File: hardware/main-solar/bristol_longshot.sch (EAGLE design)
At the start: 83 parts, among them U1 SAM_D20E, U10 TPS62243, U11 TPS3808, U12 74LVC1G04GW, U13 SPV1040, U14 LT4054ES5-4.2, U2 SI4060, U3 UBLOX_MAX, U4 TPS62243, U5 TG-5006CJ, U6 TG-5006CJ, U7 TPS3123, U8 SN74LVC1G32DCKR, U9 SE880, Y1 ABS05

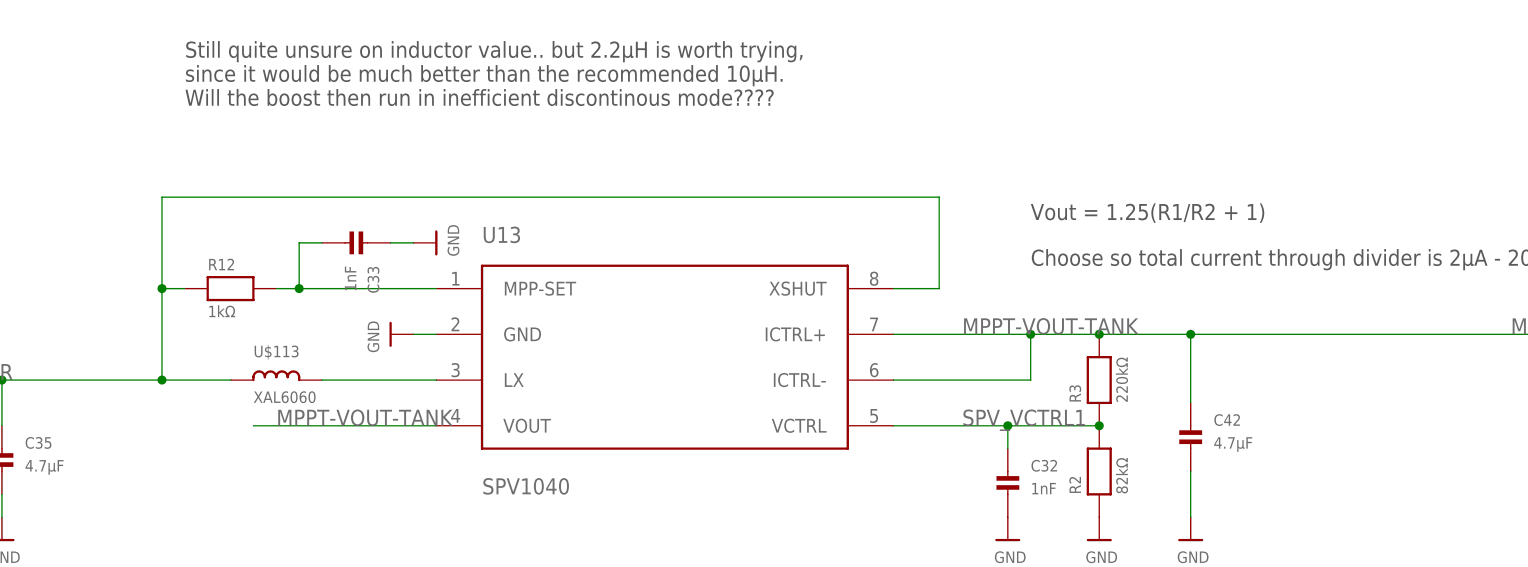
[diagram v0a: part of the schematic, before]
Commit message: Added LPS3015 mppt inductor footprint alongside XAL6060 footprint
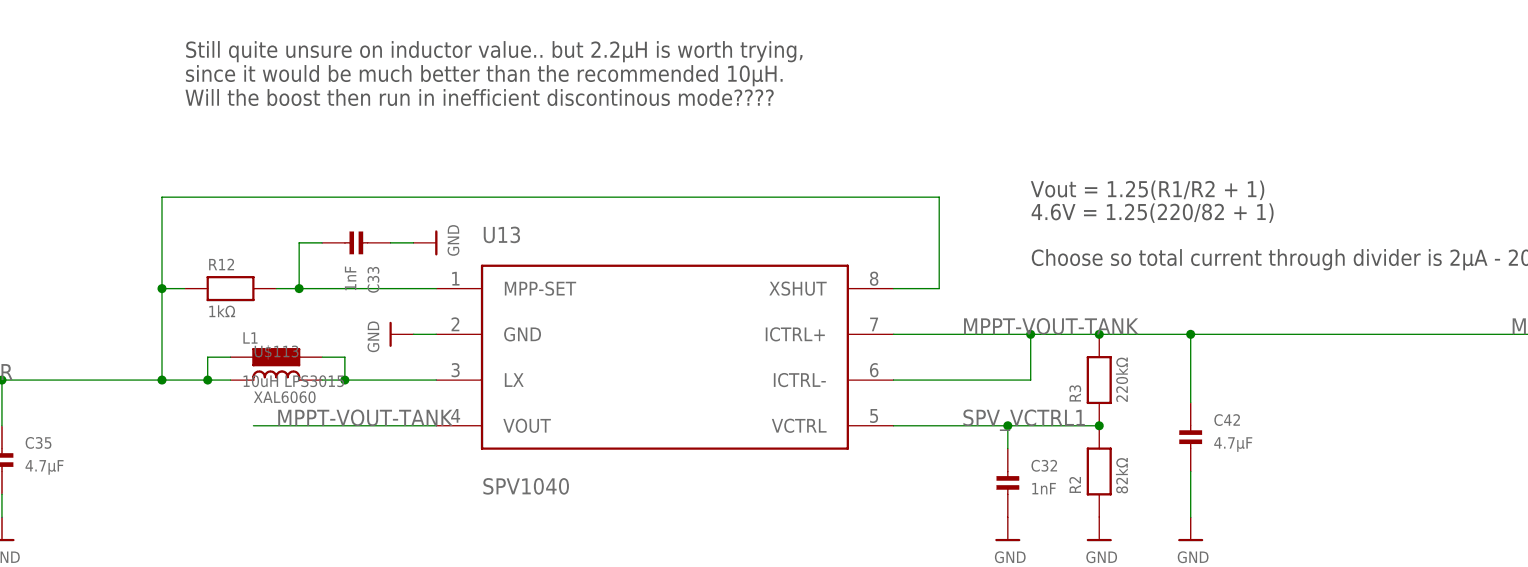
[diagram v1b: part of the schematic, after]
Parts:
- added L1: 10uH LPS3015, PecanFemto4:IND-LPS3015
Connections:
- net LX1: now also L1.2
- net VSOLAR: now also L1.1
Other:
- note added: "4.6V = 1.25(220/82 + 1)"
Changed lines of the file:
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@@
 <layer number="54" name="bGND_GNDA" color="1" fill="9" visible="no" active="no"/>
 <layer number="56" name="wert" color="7" fill="1" visible="no" active="no"/>
+<layer number="57" name="tCAD" color="7" fill="1" visible="no" active="no"/>
 <layer number="90" name="Modules" color="5" fill="1" visible="yes" active="yes"/>
 <layer number="91" name="Nets" color="2" fill="1" visible="yes" active="yes"/>
@@
 <layer number="97" name="Info" color="7" fill="1" visible="yes" active="yes"/>
 <layer number="98" name="Guide" color="6" fill="1" visible="yes" active="yes"/>
+<layer number="99" name="SpiceOrder" color="7" fill="1" visible="yes" active="yes"/>
 <layer number="100" name="Muster" color="7" fill="1" visible="no" active="no"/>
 <layer number="101" name="Patch_Top" color="12" fill="4" visible="yes" active="yes"/>
@@
 <layer number="111" name="LPC17xx" color="7" fill="1" visible="yes" active="yes"/>
 <layer number="112" name="tSilk" color="7" fill="1" visible="yes" active="yes"/>
+<layer number="113" name="IDFDebug" color="4" fill="1" visible="yes" active="yes"/>
 <layer number="116" name="Patch_BOT" color="9" fill="4" visible="yes" active="yes"/>
 <layer number="121" name="_tsilk" color="7" fill="1" visible="yes" active="yes"/>
@@
 <layer number="132" name="bAdjust" color="7" fill="1" visible="no" active="yes"/>
 <layer number="144" name="Drill_legend" color="7" fill="1" visible="yes" active="yes"/>
+<layer number="150" name="Notes" color="7" fill="1" visible="yes" active="yes"/>
 <layer number="151" name="HeatSink" color="7" fill="1" visible="yes" active="yes"/>
 <layer number="152" name="_bDocu" color="7" fill="1" visible="yes" active="yes"/>
+<layer number="153" name="FabDoc1" color="7" fill="1" visible="yes" active="yes"/>
+<layer number="154" name="FabDoc2" color="7" fill="1" visible="yes" active="yes"/>
+<layer number="155" name="FabDoc3" color="7" fill="1" visible="yes" active="yes"/>
 <layer number="199" name="Contour" color="7" fill="1" visible="yes" active="yes"/>
 <layer number="200" name="200bmp" color="1" fill="10" visible="no" active="no"/>
@@
 <part name="C42" library="microbuilder_v3" deviceset="CAP_CERAMIC" device="_0402" value="4.7µF"/>
 <part name="R21" library="microbuilder_v3" deviceset="RESISTOR" device="_0402" value="DNP"/>
+<part name="L1" library="PecanFemto4" deviceset="IND-LPS3015" device="" value="10uH LPS3015"/>
 </parts>
 <sheets>
@@
 <text x="347.98" y="-114.3" size="1.778" layer="97">Rchg = 2.2kΩ gives Ichg = 70mA</text>
 <text x="347.98" y="-119.38" size="1.778" layer="97">Ichg can be measured by Vprog</text>
-<text x="165.1" y="-45.72" size="1.778" layer="97">Vout = 1.25(R1/R2 + 1)</text>
+<text x="165.1" y="-43.18" size="1.778" layer="97">Vout = 1.25(R1/R2 + 1)</text>
 <text x="165.1" y="-50.8" size="1.778" layer="97">Choose so total current through divider is 2µA - 20µA</text>
 <text x="7.62" y="-50.8" size="1.778" layer="97">Not actually an SMA connector</text>
 <text x="96.52" y="81.788" size="1.27" layer="97" font="vector" ratio="11">(AIN[0])</text>
 <text x="96.52" y="76.708" size="1.27" layer="97" font="vector" ratio="11">(AIN[4])</text>
+<text x="165.1" y="-45.72" size="1.778" layer="97">4.6V = 1.25(220/82 + 1)</text>
 </plain>
 <instances>
@@
 <instance part="C42" gate="G$1" x="182.88" y="-71.12"/>
 <instance part="R21" gate="G$1" x="378.46" y="-48.26"/>
+<instance part="L1" gate="G$1" x="81.28" y="-60.96"/>
 </instances>
 <busses>
@@
 <net name="VSOLAR" class="0">
 <segment>
-<wire x1="76.2" y1="-63.5" x2="68.58" y2="-63.5" width="0.1524" layer="91"/>
+<wire x1="76.2" y1="-63.5" x2="73.66" y2="-63.5" width="0.1524" layer="91"/>
 <label x="43.18" y="-63.5" size="1.778" layer="95"/>
 <pinref part="R12" gate="G$1" pin="1"/>
+<wire x1="73.66" y1="-63.5" x2="68.58" y2="-63.5" width="0.1524" layer="91"/>
 <wire x1="68.58" y1="-63.5" x2="50.8" y2="-63.5" width="0.1524" layer="91"/>
 <wire x1="50.8" y1="-63.5" x2="40.64" y2="-63.5" width="0.1524" layer="91"/>
@@
 <junction x="40.64" y="-63.5"/>
 <wire x1="25.4" y1="-63.5" x2="40.64" y2="-63.5" width="0.1524" layer="91"/>
+<pinref part="L1" gate="G$1" pin="1"/>
+<wire x1="76.2" y1="-60.96" x2="73.66" y2="-60.96" width="0.1524" layer="91"/>
+<wire x1="73.66" y1="-60.96" x2="73.66" y2="-63.5" width="0.1524" layer="91"/>
+<junction x="73.66" y="-63.5"/>
 </segment>
 <segment>
@@
 <segment>
 <pinref part="U13" gate="G$1" pin="LX"/>
-<wire x1="86.36" y1="-63.5" x2="99.06" y2="-63.5" width="0.1524" layer="91"/>
+<wire x1="86.36" y1="-63.5" x2="88.9" y2="-63.5" width="0.1524" layer="91"/>
 <pinref part="U$113" gate="G$1" pin="2"/>
-</segment>
-</net>
+<pinref part="L1" gate="G$1" pin="2"/>
+<wire x1="88.9" y1="-63.5" x2="99.06" y2="-63.5" width="0.1524" layer="91"/>
+<wire x1="86.36" y1="-60.96" x2="88.9" y2="-60.96" width="0.1524" layer="91"/>
+<wire x1="88.9" y1="-60.96" x2="88.9" y2="-63.5" width="0.1524" layer="91"/>
+<junction x="88.9" y="-63.5"/>
+</segment>
+</net>

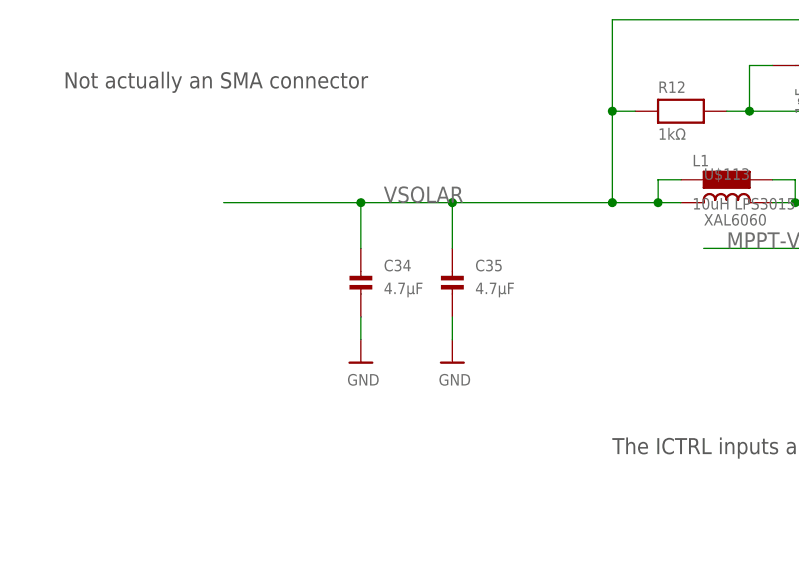
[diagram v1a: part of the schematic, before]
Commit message: Added 0603 cap to vsolar
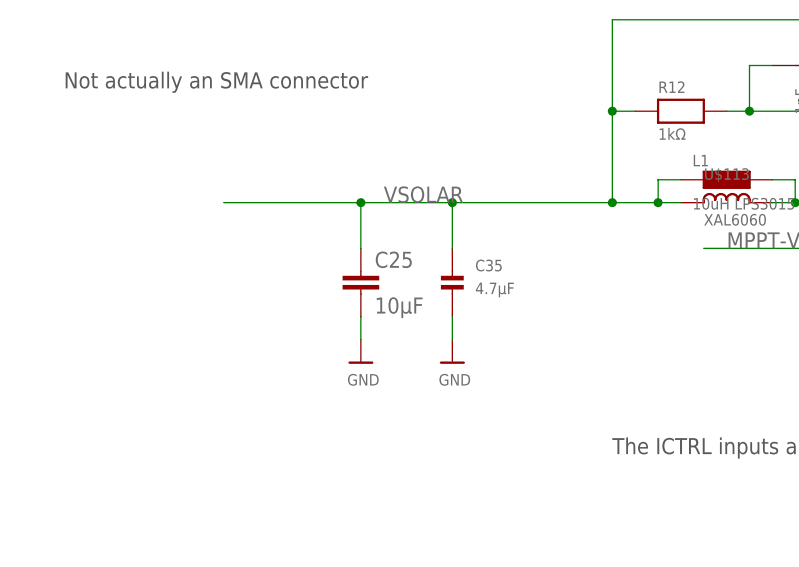
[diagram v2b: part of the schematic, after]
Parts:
- removed C34: 4.7µF, microbuilder_v3:CAP_CERAMIC_0402
- added C25: 10µF, resistor:C-EUC0603K
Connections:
- net GND: now also C25.2; no longer C34.P$2
- net VSOLAR: now also C25.1; no longer C34.P$1
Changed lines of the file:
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@@
 <part name="R12" library="microbuilder_v3" deviceset="RESISTOR" device="_0402" value="1kΩ"/>
 <part name="FRAME6" library="SparkFun" deviceset="FRAME-LETTER" device=""/>
-<part name="C34" library="microbuilder_v3" deviceset="CAP_CERAMIC" device="_0402" value="4.7µF"/>
 <part name="C35" library="microbuilder_v3" deviceset="CAP_CERAMIC" device="_0402" value="4.7µF"/>
 <part name="U$104" library="microbuilder_v3" deviceset="GND" device=""/>
@@
 <part name="R21" library="microbuilder_v3" deviceset="RESISTOR" device="_0402" value="DNP"/>
 <part name="L1" library="PecanFemto4" deviceset="IND-LPS3015" device="" value="10uH LPS3015"/>
+<part name="C25" library="resistor" deviceset="C-EU" device="C0603K" value="10µF"/>
 </parts>
 <sheets>
@@
 <instance part="FRAME6" gate="G$1" x="251.46" y="-187.96"/>
 <instance part="FRAME6" gate="G$2" x="396.24" y="-187.96"/>
-<instance part="C34" gate="G$1" x="40.64" y="-73.66"/>
 <instance part="C35" gate="G$1" x="50.8" y="-73.66"/>
 <instance part="U$104" gate="G$1" x="40.64" y="-81.28"/>
@@
 <instance part="R21" gate="G$1" x="378.46" y="-48.26"/>
 <instance part="L1" gate="G$1" x="81.28" y="-60.96"/>
+<instance part="C25" gate="G$1" x="40.64" y="-71.12"/>
 </instances>
 <busses>
@@
 </segment>
 <segment>
-<pinref part="U$104" gate="G$1" pin="GND"/>
-<pinref part="C34" gate="G$1" pin="P$2"/>
-<wire x1="40.64" y1="-78.74" x2="40.64" y2="-76.2" width="0.1524" layer="91"/>
-</segment>
-<segment>
 <pinref part="U$105" gate="G$1" pin="GND"/>
 <pinref part="C35" gate="G$1" pin="P$2"/>
@@
 <pinref part="C42" gate="G$1" pin="P$2"/>
 <wire x1="182.88" y1="-73.66" x2="182.88" y2="-78.74" width="0.1524" layer="91"/>
+</segment>
+<segment>
+<pinref part="C25" gate="G$1" pin="2"/>
+<wire x1="40.64" y1="-78.74" x2="40.64" y2="-76.2" width="0.1524" layer="91"/>
+<pinref part="U$104" gate="G$1" pin="GND"/>
 </segment>
 </net>
@@
 <pinref part="C35" gate="G$1" pin="P$1"/>
 <wire x1="50.8" y1="-68.58" x2="50.8" y2="-63.5" width="0.1524" layer="91"/>
-<pinref part="C34" gate="G$1" pin="P$1"/>
 <wire x1="40.64" y1="-68.58" x2="40.64" y2="-63.5" width="0.1524" layer="91"/>
 <junction x="50.8" y="-63.5"/>
@@
 <wire x1="73.66" y1="-60.96" x2="73.66" y2="-63.5" width="0.1524" layer="91"/>
 <junction x="73.66" y="-63.5"/>
-</segment>
-<segment>
+<pinref part="C25" gate="G$1" pin="1"/>
+</segment>
+<segment>

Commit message: Updated many parts lists, updated bard numbering, removed makefiles for inactive things
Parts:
- removed C38, C39: 4.7µF, microbuilder_v3:CAP_CERAMIC_0402
- removed C40: 1nF, microbuilder_v3:CAP_CERAMIC_0402
- removed C41: 10µF, resistor:C-EUC0603K
- removed R19: 10kΩ, microbuilder_v3:RESISTOR_0402
- removed U$19: SST25WF040BT-40I/NP, fbri:SST25WF040BT-40I/NP
- added C24, C26: 10µF, resistor:C-EUC0603K
- added C27: 4.7µF, microbuilder_v3:CAP_CERAMIC_0402
- added C34: 1nF, microbuilder_v3:CAP_CERAMIC_0402
- added R13: 75kΩ/82kΩ, microbuilder_v3:RESISTOR_0402
- added U15: 74LVC1G04GW, 74LVC1G04GW_inverter:74LVC1G04GW
- C31: value 10µF -> 4.7µF; device resistor:C-EUC0603K -> microbuilder_v3:CAP_CERAMIC_0402
- C32: value 1nF -> 4.7µF
- C35: value 4.7µF -> 1nF
- R11: value 10kΩ -> 1kΩ
- R12: value 1kΩ -> 180kΩ/220kΩ
- R15: value DNP -> 0Ω/DNP
- R2: value 82kΩ -> 10kΩ
- R3: value 220kΩ -> 10kΩ
- U10: value TPS62243 -> SPV1040; device TPS62243:TPS62243 -> spv1040:SPV1040
- U11: value TPS3808 -> LT4054ES5-4.2; device TPS3808:TPS3808 -> XYKlib:LT4054ES5-4.2
- U12: value 74LVC1G04GW -> TPS62243; device 74LVC1G04GW_inverter:74LVC1G04GW -> TPS62243:TPS62243
- U13: value SPV1040 -> TPS62243; device spv1040:SPV1040 -> TPS62243:TPS62243
- U14: value LT4054ES5-4.2 -> TPS3808; device XYKlib:LT4054ES5-4.2 -> TPS3808:TPS3808
- U4: value TPS62243 -> SST25WF040BT-40I/NP; device TPS62243:TPS62243 -> fbri:SST25WF040BT-40I/NP
- renumbered C36 to C30, C37 to C29, C42 to C28, L1 to L1B, R18 to R14, R21 to R15, U$113 to L1A, U$74 to JTAG1
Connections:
- net 1.8V: now also C25.1, C26.1, U12.FB, U13.FB, U4.VDD; no longer C31.1, C41.1, U$19.VDD, U10.FB, U4.FB
- net BATTERY: now also C32.P$1, U11.BAT, U13.VIN; no longer C38.P$1, U14.BAT, U4.VIN
- net BATTERY_BUCK_SW: now also U13.SW; no longer U4.SW
- net BATTERY_EN: now also R7.1, U13.EN, U15.Y; no longer R11.1, U12.Y, U4.EN
- net CHG_STATUS: now also U11.CHRG; no longer U14.CHRG
- net CT: now also U14.CT; no longer U11.CT
- net GND: now also C24.2, C26.2, C27.P$2, C31.P$2, C34.P$2, R13.1, R3.1, U12.GND2, U12.MODE, U13.GND2, U13.MODE, U14.GND2, U15.GND, U4.GND_PAD, U4.VSS; no longer C31.2, C38.P$2, C39.P$2, C40.P$2, C41.2, R6.1, R7.1, U$19.GND_PAD, U$19.VSS, U10.GND2, U10.MODE, U11.GND2, U4.GND, U4.GND2, U4.MODE
- net LX1: now also U10.LX; no longer U13.LX
- net MEM_CSN: now also U4.CSN; no longer U$19.CSN
- net MEM_MISO: now also U4.SO/IO1; no longer U$19.SO/IO1
- net MEM_MOSI: now also U4.SI/IO0; no longer U$19.SI/IO0
- net MEM_SCK: now also U4.SCK; no longer U$19.SCK
- net MEM_WPN: now also U4.WPN/IO2; no longer U$19.WPN/IO2
- net MPP-SET: now also R11.2, U10.MPP-SET; no longer R12.2, U13.MPP-SET
- net MPPT-VOUT-TANK: now also C31.P$1, R12.2, U10.ICTRL+, U10.ICTRL-, U10.VOUT, U11.VCC, U12.VIN, U14.SENSE; no longer C39.P$1, R3.2, U10.VIN, U11.SENSE, U13.ICTRL+, U13.ICTRL-, U13.VOUT, U14.VCC
- net N$3: now also R3.2; no longer R6.2
- net N$5: now also R2.2; no longer R5.2
- net PROG: now also U11.PROG; no longer U14.PROG
- net SPV_VCTRL1: now also C34.P$1, R12.1, R13.2, U10.VCTRL; no longer C32.P$1, R2.2, R3.1, U13.VCTRL
- net SUPERVISOR_VCC: now also C35.P$1, R6.2, R7.2, U14.VDD, U15.VCC; no longer C40.P$1, R11.2, R19.2, U11.VDD, U12.VCC
- net TANK_BUCK_SW: now also U12.SW; no longer U10.SW
- net TANK_EN: now also R6.1, U12.EN, U14.!RESET, U15.A; no longer R19.1, U10.EN, U11.!RESET, U12.A
- net VBATT_SENSE: now also R5.2; no longer R7.2
- net VSOLAR: now also C24.1, C27.P$1, R11.1, U10.XSHUT; no longer C25.1, C35.P$1, R12.1, U13.XSHUT
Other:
- note added: "4.25V = 1.25(180/75 + 1)"
- note added: "4.60V = 1.25(220/82 + 1)"
- note added: "Place"
- note removed: "4.6V = 1.25(220/82 + 1)"
- moved on the sheet: C25, C31, C32, C35, R11, R12, R2, R3, R5, R6, R7

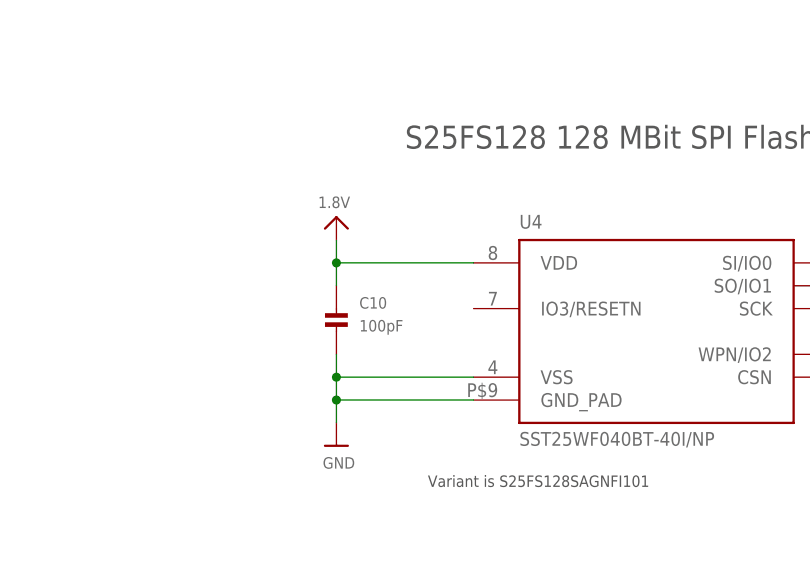
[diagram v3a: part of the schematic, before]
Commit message: [Bugfix] Memory HOLD pin needs to be high. Also adjusted pad/cream size. Bump to V0.98x.1
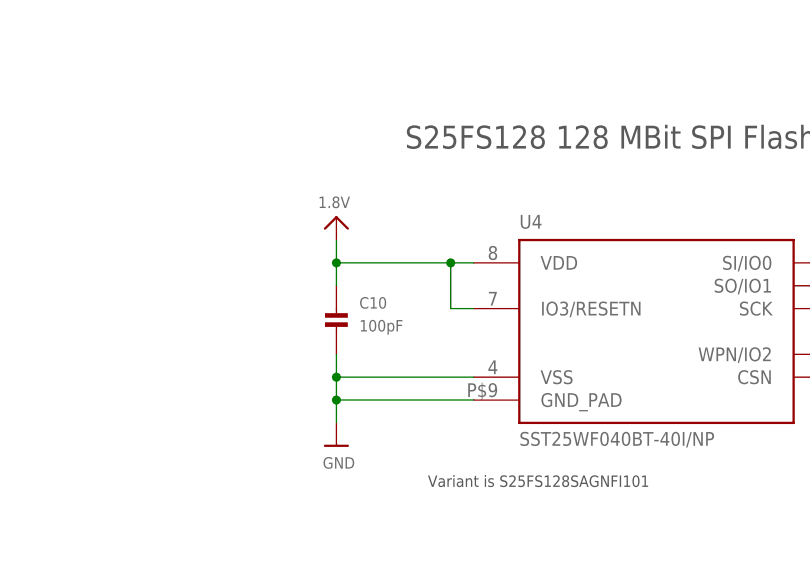
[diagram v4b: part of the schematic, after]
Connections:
- net 1.8V: now also U4.IO3/RESETN
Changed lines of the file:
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@@
 <segment>
 <pinref part="U$40" gate="G$1" pin="1.8V"/>
-<wire x1="81.28" y1="33.02" x2="66.04" y2="33.02" width="0.1524" layer="91"/>
+<wire x1="81.28" y1="33.02" x2="78.74" y2="33.02" width="0.1524" layer="91"/>
+<wire x1="78.74" y1="33.02" x2="66.04" y2="33.02" width="0.1524" layer="91"/>
 <wire x1="66.04" y1="33.02" x2="66.04" y2="35.56" width="0.1524" layer="91"/>
 <pinref part="C10" gate="G$1" pin="P$1"/>
@@
 <junction x="66.04" y="33.02"/>
 <pinref part="U4" gate="G$1" pin="VDD"/>
+<pinref part="U4" gate="G$1" pin="IO3/RESETN"/>
+<wire x1="81.28" y1="27.94" x2="78.74" y2="27.94" width="0.1524" layer="91"/>
+<wire x1="78.74" y1="27.94" x2="78.74" y2="33.02" width="0.1524" layer="91"/>
+<junction x="78.74" y="33.02"/>
 </segment>
 <segment>
